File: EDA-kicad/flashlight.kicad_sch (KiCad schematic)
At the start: 3 parts, among them U10 Flash-LED-Lumiled

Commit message: POWER SCHEMATIC FINISHED
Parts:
- Q4: renamed from Q3; MPN (none) -> BSS816NWH6327XTSA1
- renumbered R22 to R25

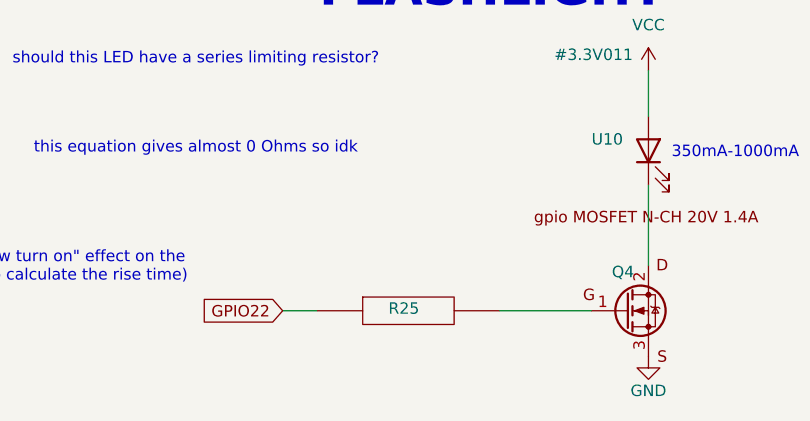
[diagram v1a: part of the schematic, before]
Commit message: assign power section footprints and import to pcb
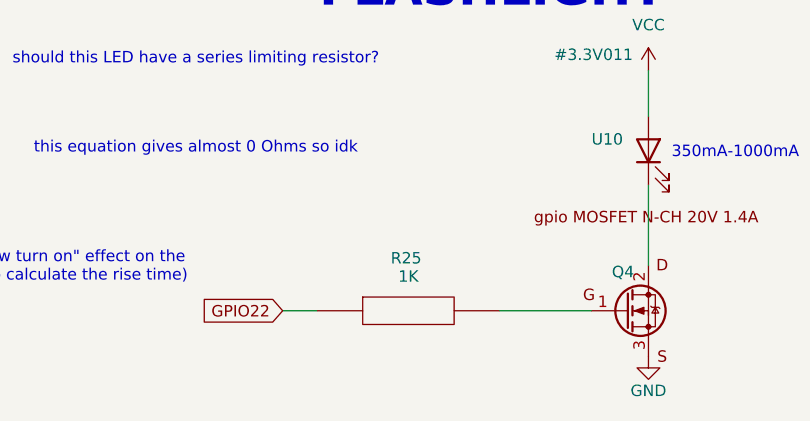
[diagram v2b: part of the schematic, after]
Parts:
- R25: value 1K-05W-0805-RES_ERJP06J102V -> 1K; MPN (none) -> ERJ-P06J102V

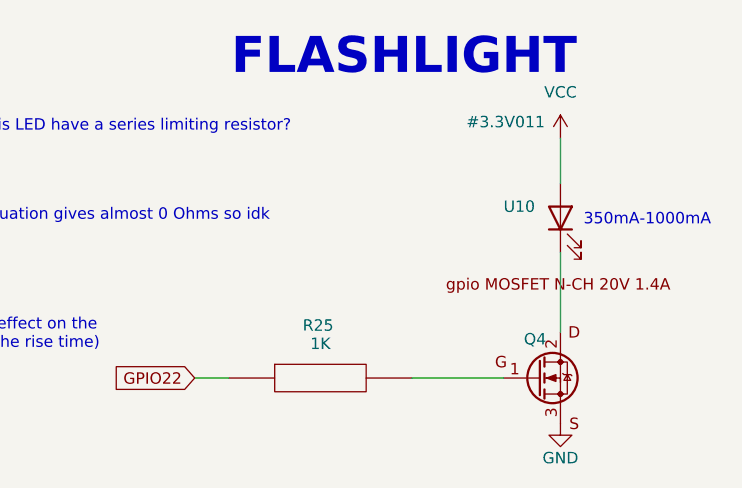
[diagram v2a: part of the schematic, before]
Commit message: set everything except from power to DNP
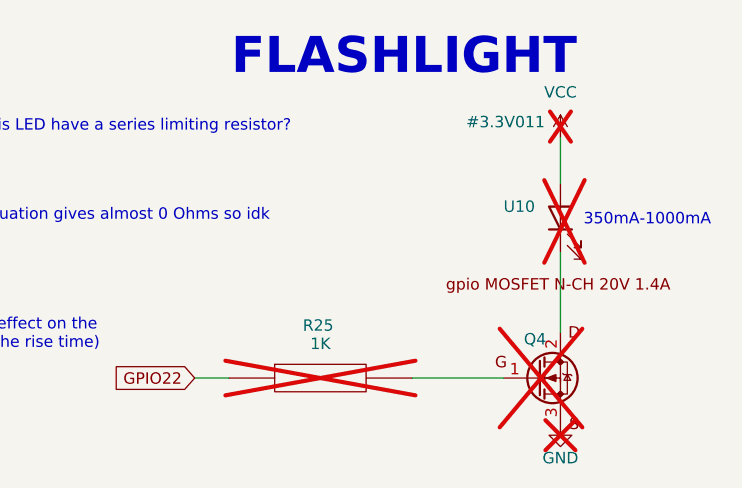
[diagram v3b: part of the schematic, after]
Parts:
- Q4, R25, U10: now not fitted

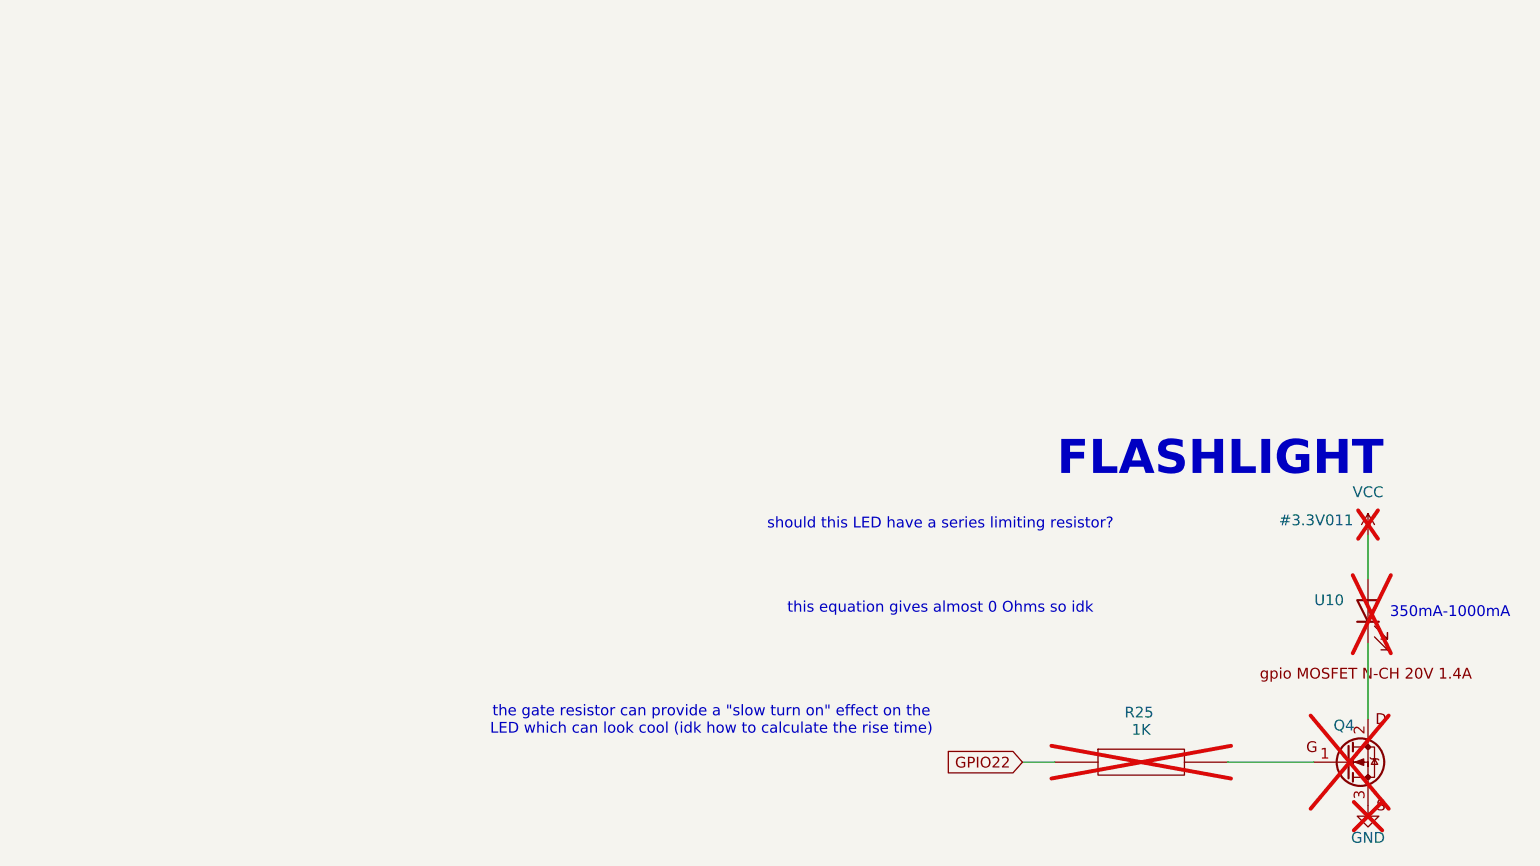
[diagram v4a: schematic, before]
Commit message: Reduced the GPIO usage for the Buttons and redone the LED
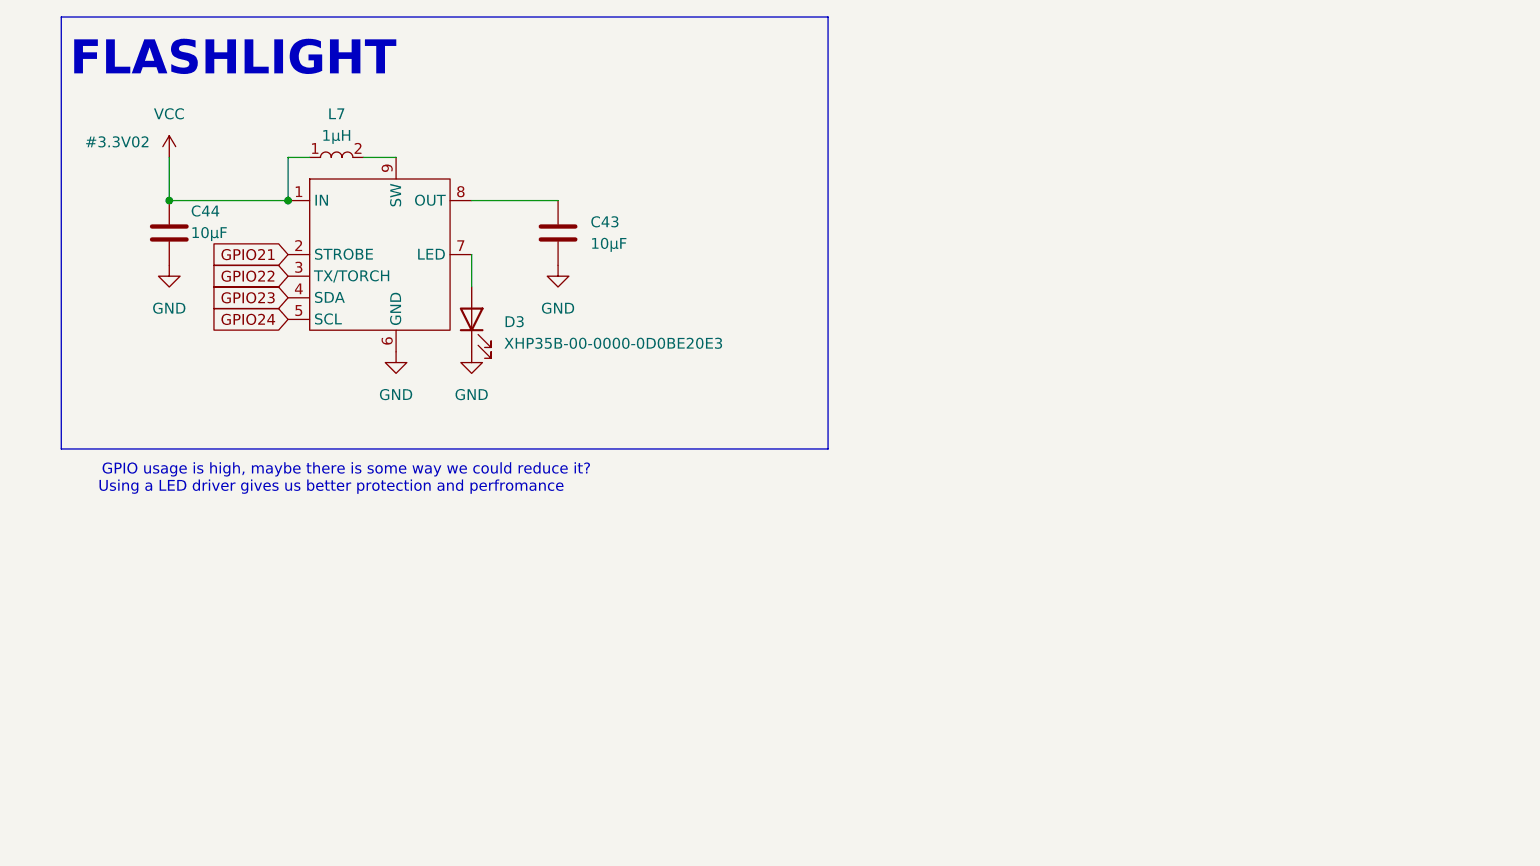
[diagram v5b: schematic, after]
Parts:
- removed Q4: ~, SPIRIT-footprints:gpio-driver-transistor-fix-SOT65P210X110-3N, symbol SPIRIT-components:gpio-driver-transistor-BSS816NWH6327XTSA1
- removed R25: 1K, SPIRIT-footprints:1K-05W-0805-RES_ERJP06J102V, symbol SPIRIT-components:1K-05W-0805-RES_ERJP06J102V
- removed U10: Flash-LED-Lumiled, SPIRIT-footprints:LUMILED-DIODFN449X305X210-3N, symbol SPIRIT-components:Flash-LED-Lumiled
- added C43, C44: 10μF, symbol Device:C
- added D3: XHP35B-00-0000-0D0BE20E3, symbol Device:LED
- added L7: 1μH, SPIRIT-footprints:1-5uH-inductor-VLS5030EX-D, symbol SPIRIT-components:1-5uH-inductor-VLS5030EX-D
- added U11: ~, symbol TI_LM3642:LM3642
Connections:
- net GND: now also C43.2, C44.2, D3.1 (K), U11.6 (GND)
- net GPIO22: now also U11.3 (TX/TORCH)
- net VCC: now also C44.1, L7.1, U11.1 (IN)
- new net: D3.2 (A), U11.7 (LED)
- new net: L7.2, U11.9 (SW)
- new net: C43.1, U11.8 (OUT)
- new net GPIO21: U11.2 (STROBE)
- new net GPIO23: U11.4 (SDA)
- new net GPIO24: U11.5 (SCL)
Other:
- note added: "GPIO usage is high, maybe there is some way we could reduce it?"
- note added: "Using a LED driver gives us better protection and perfromance"
- note removed: "350mA-1000mA"
- note removed: "should this LED have a series limiting resistor?"
- note removed: "the gate resistor can provide a "slow turn on" effect on the LED which can look cool (idk how to calculate the rise time)"
- note removed: "this equation gives almost 0 Ohms so idk"
